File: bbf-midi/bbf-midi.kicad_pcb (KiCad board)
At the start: 2 copper layers, 32.5 x 52.1 mm, 20 parts, among them J1 Conn_02x05_Odd_Even, J2 Conn_02x05_Odd_Even, J3 DIN-5_180degree, J4 DIN-5_180degree, J5 Conn_01x03, Q1 2N3904, U1 TLV1117-33

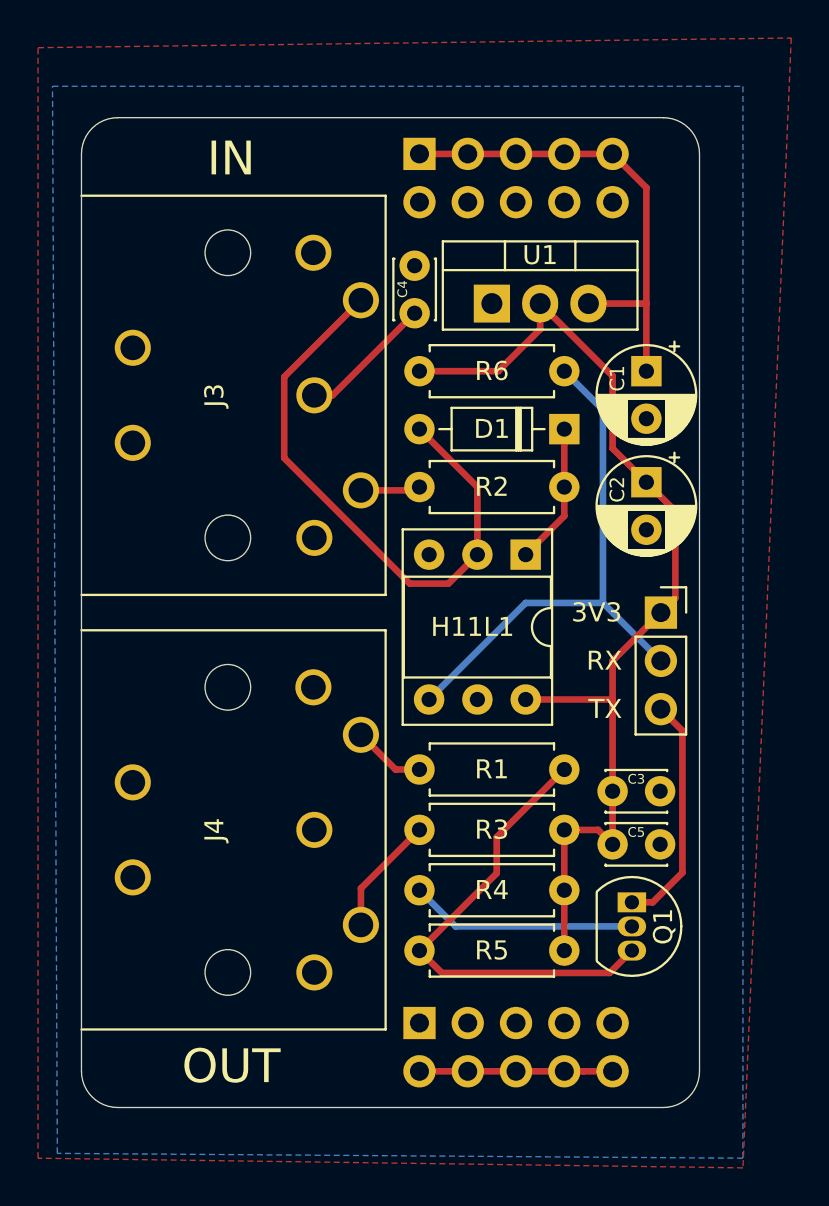
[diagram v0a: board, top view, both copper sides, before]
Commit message: Fix some small mistakes in the midi friend.
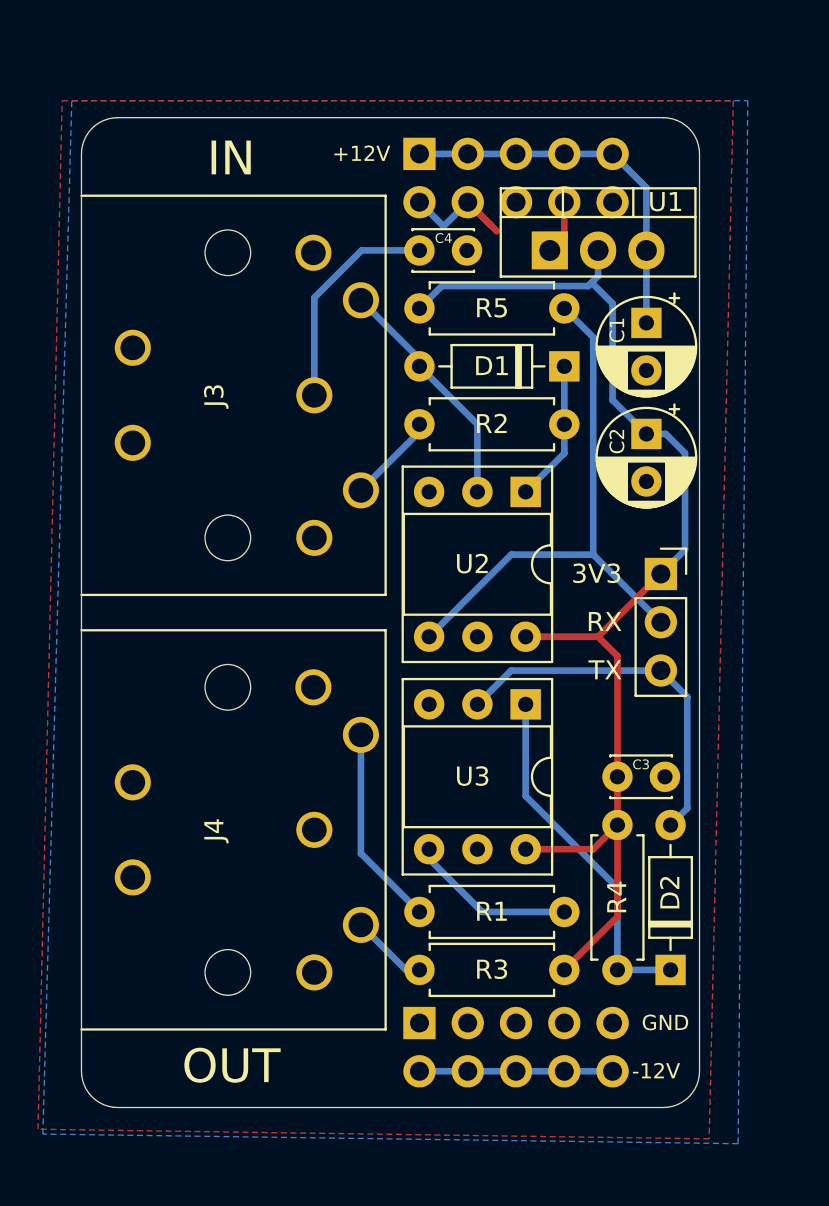
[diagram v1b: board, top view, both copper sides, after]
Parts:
- removed C5: 100n, Capacitor_THT:C_Disc_D3.0mm_W2.0mm_P2.50mm
- removed Q1: 2N3904, Package_TO_SOT_THT:TO-92_Inline
- removed R6: 1K, Resistor_THT:R_Axial_DIN0207_L6.3mm_D2.5mm_P7.62mm_Horizontal
- added D2: D_Small, Diode_THT:D_DO-35_SOD27_P7.62mm_Horizontal, F.Cu at (155.4, 131.8)
- added U3: H11L1, Package_DIP:DIP-6_W7.62mm_Socket, F.Cu at (147.8, 117.9)
- R4: value 1K -> 470
- moved R5 34.6 mm to (149.9, 97.0), turned to 180 degrees
- moved R4 11.2 mm to (152.7, 131.8), turned to 90 degrees
- moved R1 10.7 mm to (149.9, 128.8), turned to 180 degrees
- moved R3 7.37 mm to (142.2, 131.8)
- moved U1 4.13 mm to (149.1, 94.0)
- moved C4 3.31 mm to (142.2, 94.0), turned to 0 degrees
- moved D1 3.30 mm to (149.9, 100.1)
- moved R2 3.30 mm to (149.9, 103.1)
- moved U2 3.30 mm to (147.8, 106.7)
- moved C1 2.54 mm to (154.2, 97.8)
- moved C2 2.54 mm to (154.2, 103.6)
- moved J5 2.03 mm to (154.9, 111.0)
- moved C3 0.80 mm to (152.7, 121.7)
- renumbered H11L1 to U2
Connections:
- R1 pad 1: Net-(J4-Pad5) -> Net-(R1-Pad1)
- R1 pad 2: Net-(Q1-Pad3) -> Net-(J4-Pad5)
- R5 pad 1: Net-(Q1-Pad3) -> Net-(J5-Pad2)
- U1 pad 1: (no net) -> GND
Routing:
- net Net-(Q1-Pad3): track 24.8 -> 0.00 mm
- net Net-(D1-Pad2): track 31.4 -> 12.6 mm
- net GND: track 0.00 -> 10.4 mm
- net Net-(R1-Pad1): track 0.00 -> 8.78 mm
- net VCC: track 55.2 -> 62.9 mm
- net Net-(D2-Pad2): track 12.4 -> 19.5 mm
- net Net-(D2-Pad1): track 12.0 -> 18.8 mm
- net Net-(J4-Pad5): track 3.84 -> 10.6 mm
- net +12V: track 25.4 -> 19.8 mm
- net Net-(C4-Pad1): track 7.06 -> 11.7 mm
- net Net-(J4-Pad4): track 6.28 -> 4.06 mm
- net Net-(J3-Pad4): track 3.15 -> 4.75 mm
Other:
- board text added: "+12V"
- board text added: "-12V"
- board text added: "GND"
- board text added: "JLCJLCJLCJLC"
- board text added: "MIDI Breadboard Friend v1.0 cc-by-sa David Stalnaker 2020"
